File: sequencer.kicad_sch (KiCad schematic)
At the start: 68 parts, among them J1 AudioJack2, J2 AudioJack2_Switch, J3 AudioJack2, J4 Conn_ARM_JTAG_SWD_10, J5 Conn_01x06_Male, SW1 OS102011MS2QN1, SW10 OS102011MS2QN1, SW2 OS102011MS2QN1, SW3 OS102011MS2QN1, SW4 OS102011MS2QN1, SW5 OS102011MS2QN1, SW6 OS102011MS2QN1, SW7 OS102011MS2QN1, SW8 OS102011MS2QN1, U1 LM358, U2 74HC4051, U3 STM32F031K6Tx, U4 74HC14, U5 LM7805_TO220, U7 L78L33_SOT89, X1 ASV-8.000MHz

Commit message: Complete TODOs
- assign all footprints except pots
- hook up duty cycle pot
- add power switch
- switch to HCT inverters for logic level compatibility with 3.3V CMOS
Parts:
- removed J1, J3: AudioJack2, symbol Connector_Audio:AudioJack2
- removed J2: AudioJack2_Switch, symbol Connector_Audio:AudioJack2_Switch
- removed U5: LM7805_TO220, Package_TO_SOT_THT:TO-220-3_Vertical, symbol Regulator_Linear:LM7805_TO220
- added C27, C29, C31: 100n, Capacitor_SMD:C_0603_1608Metric, symbol Device:C
- added C28, C30: 330n, Capacitor_SMD:C_0805_2012Metric, symbol Device:C
- added J1, J2, J3: AudioJack2_SwitchT, Connector_Audio:Jack_3.5mm_QingPu_WQP-PJ398SM_Vertical_CircularHoles, symbol Connector_Audio:AudioJack2_SwitchT
- added J6: Conn_01x02_Male, Connector_Molex:Molex_SL_171971-0002_1x02_P2.54mm_Vertical, symbol Connector:Conn_01x02_Male
- added RV10: 10k, symbol Device:R_Potentiometer
- added SW10: SW_SPST, Button_Switch_THT_gkeeth:SW_Toggle_SPST_NKK_M2011xxx03, symbol Switch:SW_SPST
- added U5: L78L05_SOT89, Package_TO_SOT_SMD:SOT-89-3, symbol Regulator_Linear:L78L05_SOT89
- D9: footprint LED_SMD:LED_0603_1608Metric_Castellated -> LED_SMD:LED_0603_1608Metric
- J5: footprint (none) -> Connector_PinHeader_2.54mm:PinHeader_1x06_P2.54mm_Vertical
- U1: footprint (none) -> Package_SO:SOIC-8_3.9x4.9mm_P1.27mm
- U2: footprint (none) -> Package_SO:SOIC-16_3.9x9.9mm_P1.27mm
- U4: value 74HC14 -> 74HCT14; footprint (none) -> Package_SO:SOIC-14_3.9x8.7mm_P1.27mm
- renumbered C13 to C26, SW10 to SW9, U7 to U6
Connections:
- net clock_out_unbuffered is gone; now on net selected_clock_buffered: U4.5
- net +3.3V: now also U6.1 (OUT), C31.2, RV10.1
- net +5V: now also SW9.1 (A), C29.2, U5.1 (OUT)
- net +9V: now also U6.3 (IN), C28.1, C30.1, SW10.2 (B), U5.3 (IN)
- net GND: now also SW9.3 (C), U6.2 (GND), C27.1, C28.2, C29.1, C30.2, C31.1, J1.S, J2.S, J3.S, J6.2 (Pin_2), RV10.3, U5.2 (GND)
- net clock_out_buffered: now also J3.T
- net cv_out_buffered: now also J2.T
- net internal_clock: now also U3.21 (PA11), J1.TN; no longer U3.14 (PB0)
- net selected_clock_unbuffered: now also J1.T
- net skip_reset_switch: now reaches SW9.2 (B)
- net skip_reset_switch: now also U3.18 (PA8)
- new net: J6.1 (Pin_1), SW10.1 (A)
- new net duty_pot: C27.2, RV10.2, U3.14 (PB0)
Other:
- note added: "ADC_IN8"
- note added: "CV Output"
- note added: "Clock Input"
- note added: "Clock/Gate Output"
- note added: "Gate Duty Cycle Control"
- note added: "Power Switch"
- note added: "Skip/Reset Selector"
- note added: "TIM1_CH4"
- note added: "Tempo Control"
- note removed: "TIM3_CH3"
- moved on the sheet: C26, J4, R3, RV9, SW9, U4A, U4B, U4C, U4D, U6

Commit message: add footprints to pots
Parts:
- RV1, RV10, RV2, RV3, RV4, RV5, RV6, RV7, RV8, RV9: footprint (none) -> Potentiometer_THT:Potentiometer_Bourns_PTV09A-1_Single_Vertical; Distributor (none) -> Digikey; Distributor PN (none) -> PTV09A-4020F-B103-ND; Manufacturer (none) -> Bourns; Manufacturer PN (none) -> PTV09A-4020F-B103
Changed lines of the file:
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@@
       (effects (font (size 1.27 1.27)) (justify right))
     )
-    (property "Footprint" "" (at 93.98 26.67 0)
+    (property "Footprint" "Potentiometer_THT:Potentiometer_Bourns_PTV09A-1_Single_Vertical" (at 93.98 26.67 0)
       (effects (font (size 1.27 1.27)) hide)
     )
@@
       (effects (font (size 1.27 1.27)) hide)
     )
+    (property "Distributor" "Digikey" (at 93.98 26.67 0)
+      (effects (font (size 1.27 1.27)) hide)
+    )
+    (property "Distributor PN" "PTV09A-4020F-B103-ND" (at 93.98 26.67 0)
+      (effects (font (size 1.27 1.27)) hide)
+    )
+    (property "Manufacturer" "Bourns" (at 93.98 26.67 0)
+      (effects (font (size 1.27 1.27)) hide)
+    )
+    (property "Manufacturer PN" "PTV09A-4020F-B103" (at 93.98 26.67 0)
+      (effects (font (size 1.27 1.27)) hide)
+    )
     (pin "1")
     (pin "2")
@@
       (effects (font (size 1.27 1.27)) (justify right))
     )
-    (property "Footprint" "" (at 252.73 26.67 0)
+    (property "Footprint" "Potentiometer_THT:Potentiometer_Bourns_PTV09A-1_Single_Vertical" (at 252.73 26.67 0)
       (effects (font (size 1.27 1.27)) hide)
     )
@@
       (effects (font (size 1.27 1.27)) hide)
     )
+    (property "Distributor" "Digikey" (at 252.73 26.67 0)
+      (effects (font (size 1.27 1.27)) hide)
+    )
+    (property "Distributor PN" "PTV09A-4020F-B103-ND" (at 252.73 26.67 0)
+      (effects (font (size 1.27 1.27)) hide)
+    )
+    (property "Manufacturer" "Bourns" (at 252.73 26.67 0)
+      (effects (font (size 1.27 1.27)) hide)
+    )
+    (property "Manufacturer PN" "PTV09A-4020F-B103" (at 252.73 26.67 0)
+      (effects (font (size 1.27 1.27)) hide)
+    )
     (pin "1")
     (pin "2")
@@
       (effects (font (size 1.27 1.27)) (justify right))
     )
-    (property "Footprint" "" (at 62.23 26.67 0)
+    (property "Footprint" "Potentiometer_THT:Potentiometer_Bourns_PTV09A-1_Single_Vertical" (at 62.23 26.67 0)
       (effects (font (size 1.27 1.27)) hide)
     )
@@
       (effects (font (size 1.27 1.27)) hide)
     )
+    (property "Distributor" "Digikey" (at 62.23 26.67 0)
+      (effects (font (size 1.27 1.27)) hide)
+    )
+    (property "Distributor PN" "PTV09A-4020F-B103-ND" (at 62.23 26.67 0)
+      (effects (font (size 1.27 1.27)) hide)
+    )
+    (property "Manufacturer" "Bourns" (at 62.23 26.67 0)
+      (effects (font (size 1.27 1.27)) hide)
+    )
+    (property "Manufacturer PN" "PTV09A-4020F-B103" (at 62.23 26.67 0)
+      (effects (font (size 1.27 1.27)) hide)
+    )
     (pin "1")
     (pin "2")
@@
       (effects (font (size 1.27 1.27)) (justify right))
     )
-    (property "Footprint" "" (at 220.98 26.67 0)
+    (property "Footprint" "Potentiometer_THT:Potentiometer_Bourns_PTV09A-1_Single_Vertical" (at 220.98 26.67 0)
       (effects (font (size 1.27 1.27)) hide)
     )
@@
       (effects (font (size 1.27 1.27)) hide)
     )
+    (property "Distributor" "Digikey" (at 220.98 26.67 0)
+      (effects (font (size 1.27 1.27)) hide)
+    )
+    (property "Distributor PN" "PTV09A-4020F-B103-ND" (at 220.98 26.67 0)
+      (effects (font (size 1.27 1.27)) hide)
+    )
+    (property "Manufacturer" "Bourns" (at 220.98 26.67 0)
+      (effects (font (size 1.27 1.27)) hide)
+    )
+    (property "Manufacturer PN" "PTV09A-4020F-B103" (at 220.98 26.67 0)
+      (effects (font (size 1.27 1.27)) hide)
+    )
     (pin "1")
     (pin "2")
@@
       (effects (font (size 1.27 1.27)) (justify right))
     )
-    (property "Footprint" "" (at 125.73 26.67 0)
+    (property "Footprint" "Potentiometer_THT:Potentiometer_Bourns_PTV09A-1_Single_Vertical" (at 125.73 26.67 0)
       (effects (font (size 1.27 1.27)) hide)
     )
@@
       (effects (font (size 1.27 1.27)) hide)
     )
+    (property "Distributor" "Digikey" (at 125.73 26.67 0)
+      (effects (font (size 1.27 1.27)) hide)
+    )
+    (property "Distributor PN" "PTV09A-4020F-B103-ND" (at 125.73 26.67 0)
+      (effects (font (size 1.27 1.27)) hide)
+    )
+    (property "Manufacturer" "Bourns" (at 125.73 26.67 0)
+      (effects (font (size 1.27 1.27)) hide)
+    )
+    (property "Manufacturer PN" "PTV09A-4020F-B103" (at 125.73 26.67 0)
+      (effects (font (size 1.27 1.27)) hide)
+    )
     (pin "1")
     (pin "2")
@@
       (effects (font (size 1.27 1.27)) (justify right))
     )
-    (property "Footprint" "" (at 30.48 168.91 0)
+    (property "Footprint" "Potentiometer_THT:Potentiometer_Bourns_PTV09A-1_Single_Vertical" (at 30.48 168.91 0)
       (effects (font (size 1.27 1.27)) hide)
     )
@@
       (effects (font (size 1.27 1.27)) hide)
     )
+    (property "Distributor" "Digikey" (at 30.48 168.91 0)
+      (effects (font (size 1.27 1.27)) hide)
+    )
+    (property "Distributor PN" "PTV09A-4020F-B103-ND" (at 30.48 168.91 0)
+      (effects (font (size 1.27 1.27)) hide)
+    )
+    (property "Manufacturer" "Bourns" (at 30.48 168.91 0)
+      (effects (font (size 1.27 1.27)) hide)
+    )
+    (property "Manufacturer PN" "PTV09A-4020F-B103" (at 30.48 168.91 0)
+      (effects (font (size 1.27 1.27)) hide)
+    )
     (pin "1")
     (pin "2")
@@
       (effects (font (size 1.27 1.27)) (justify right))
     )
-    (property "Footprint" "" (at 30.48 26.67 0)
+    (property "Footprint" "Potentiometer_THT:Potentiometer_Bourns_PTV09A-1_Single_Vertical" (at 30.48 26.67 0)
       (effects (font (size 1.27 1.27)) hide)
     )
@@
       (effects (font (size 1.27 1.27)) hide)
     )
+    (property "Distributor" "Digikey" (at 30.48 26.67 0)
+      (effects (font (size 1.27 1.27)) hide)
+    )
+    (property "Distributor PN" "PTV09A-4020F-B103-ND" (at 30.48 26.67 0)
+      (effects (font (size 1.27 1.27)) hide)
+    )
+    (property "Manufacturer" "Bourns" (at 30.48 26.67 0)
+      (effects (font (size 1.27 1.27)) hide)
+    )
+    (property "Manufacturer PN" "PTV09A-4020F-B103" (at 30.48 26.67 0)
+      (effects (font (size 1.27 1.27)) hide)
+    )
     (pin "1")
     (pin "2")
@@
       (effects (font (size 1.27 1.27)) (justify right))
     )
-    (property "Footprint" "" (at 80.01 168.91 0)
+    (property "Footprint" "Potentiometer_THT:Potentiometer_Bourns_PTV09A-1_Single_Vertical" (at 80.01 168.91 0)
       (effects (font (size 1.27 1.27)) hide)
     )
@@
       (effects (font (size 1.27 1.27)) hide)
     )
+    (property "Distributor" "Digikey" (at 80.01 168.91 0)
+      (effects (font (size 1.27 1.27)) hide)
+    )
+    (property "Distributor PN" "PTV09A-4020F-B103-ND" (at 80.01 168.91 0)
+      (effects (font (size 1.27 1.27)) hide)
+    )
+    (property "Manufacturer" "Bourns" (at 80.01 168.91 0)
+      (effects (font (size 1.27 1.27)) hide)
+    )
+    (property "Manufacturer PN" "PTV09A-4020F-B103" (at 80.01 168.91 0)
+      (effects (font (size 1.27 1.27)) hide)
+    )
     (pin "1")
     (pin "2")
@@
       (effects (font (size 1.27 1.27)) (justify right))
     )
-    (property "Footprint" "" (at 189.23 26.67 0)
+    (property "Footprint" "Potentiometer_THT:Potentiometer_Bourns_PTV09A-1_Single_Vertical" (at 189.23 26.67 0)
       (effects (font (size 1.27 1.27)) hide)
     )
@@
       (effects (font (size 1.27 1.27)) hide)
     )
+    (property "Distributor" "Digikey" (at 189.23 26.67 0)
+      (effects (font (size 1.27 1.27)) hide)
+    )
+    (property "Distributor PN" "PTV09A-4020F-B103-ND" (at 189.23 26.67 0)
+      (effects (font (size 1.27 1.27)) hide)
+    )
+    (property "Manufacturer" "Bourns" (at 189.23 26.67 0)
+      (effects (font (size 1.27 1.27)) hide)
+    )
+    (property "Manufacturer PN" "PTV09A-4020F-B103" (at 189.23 26.67 0)
+      (effects (font (size 1.27 1.27)) hide)
+    )
     (pin "1")
     (pin "2")
@@
       (effects (font (size 1.27 1.27)) (justify right))
     )
-    (property "Footprint" "" (at 157.48 26.67 0)
+    (property "Footprint" "Potentiometer_THT:Potentiometer_Bourns_PTV09A-1_Single_Vertical" (at 157.48 26.67 0)
       (effects (font (size 1.27 1.27)) hide)
     )
@@
       (effects (font (size 1.27 1.27)) hide)
     )
+    (property "Distributor" "Digikey" (at 157.48 26.67 0)
+      (effects (font (size 1.27 1.27)) hide)
+    )
+    (property "Distributor PN" "PTV09A-4020F-B103-ND" (at 157.48 26.67 0)
+      (effects (font (size 1.27 1.27)) hide)
+    )
+    (property "Manufacturer" "Bourns" (at 157.48 26.67 0)
+      (effects (font (size 1.27 1.27)) hide)
+    )
+    (property "Manufacturer PN" "PTV09A-4020F-B103" (at 157.48 26.67 0)
+      (effects (font (size 1.27 1.27)) hide)
+    )

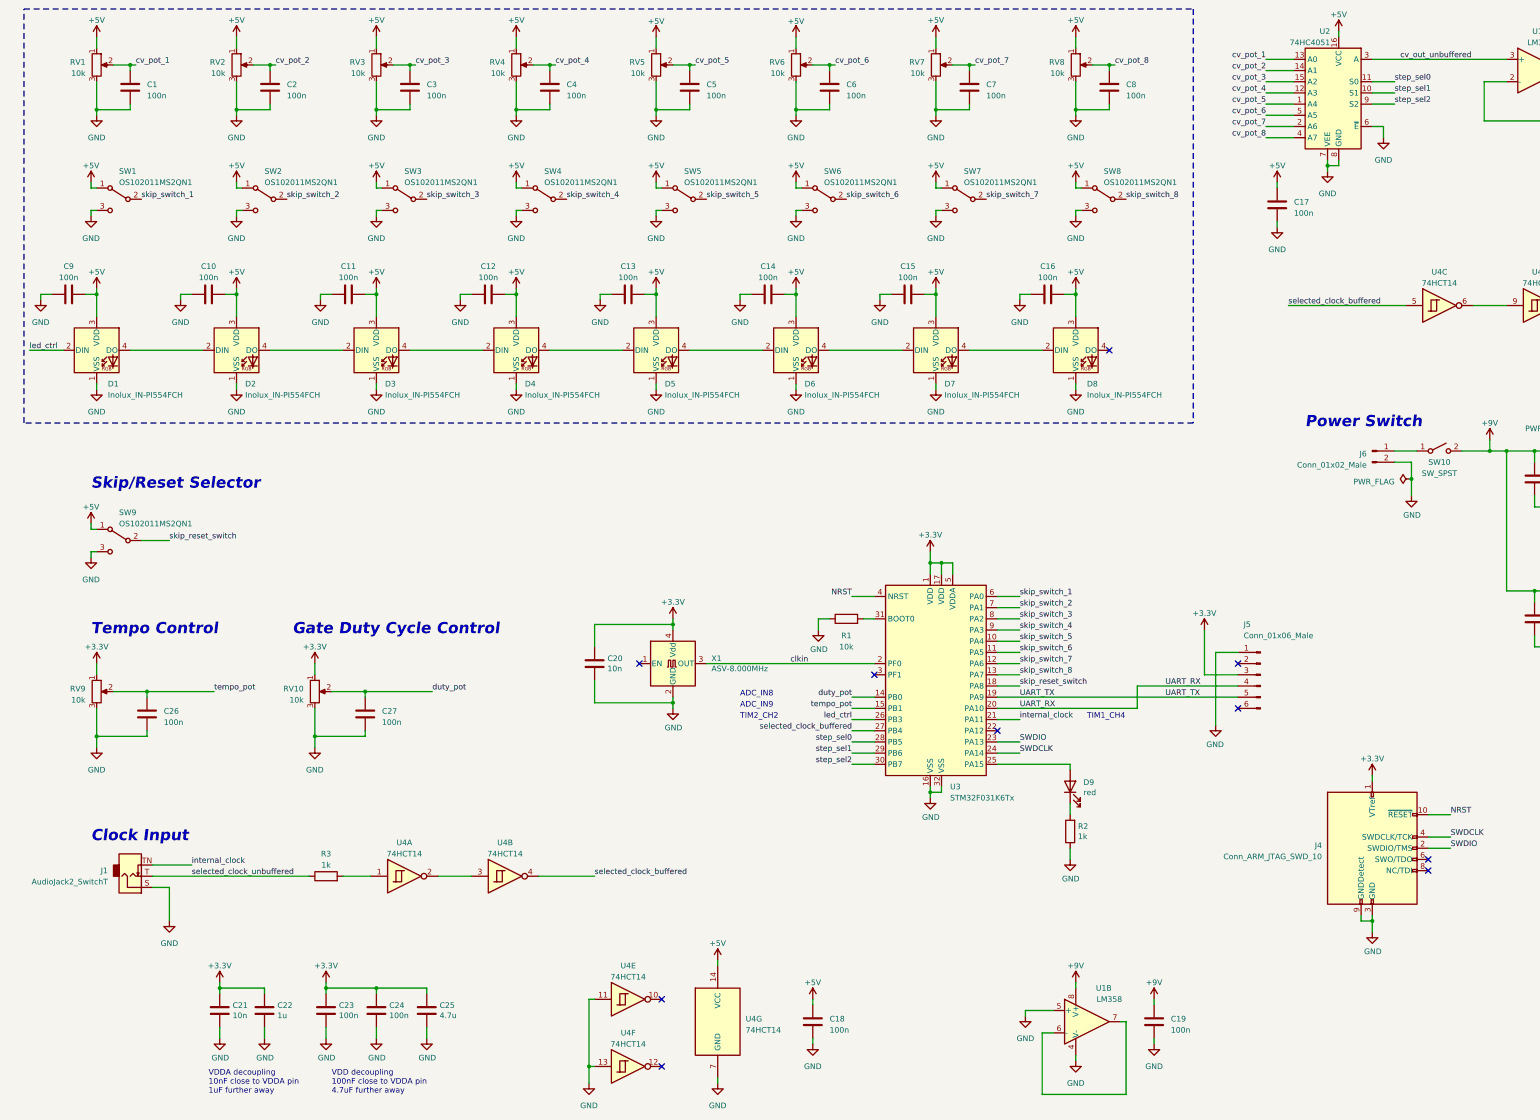
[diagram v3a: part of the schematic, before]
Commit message: initial routing complete, DRC errors clean
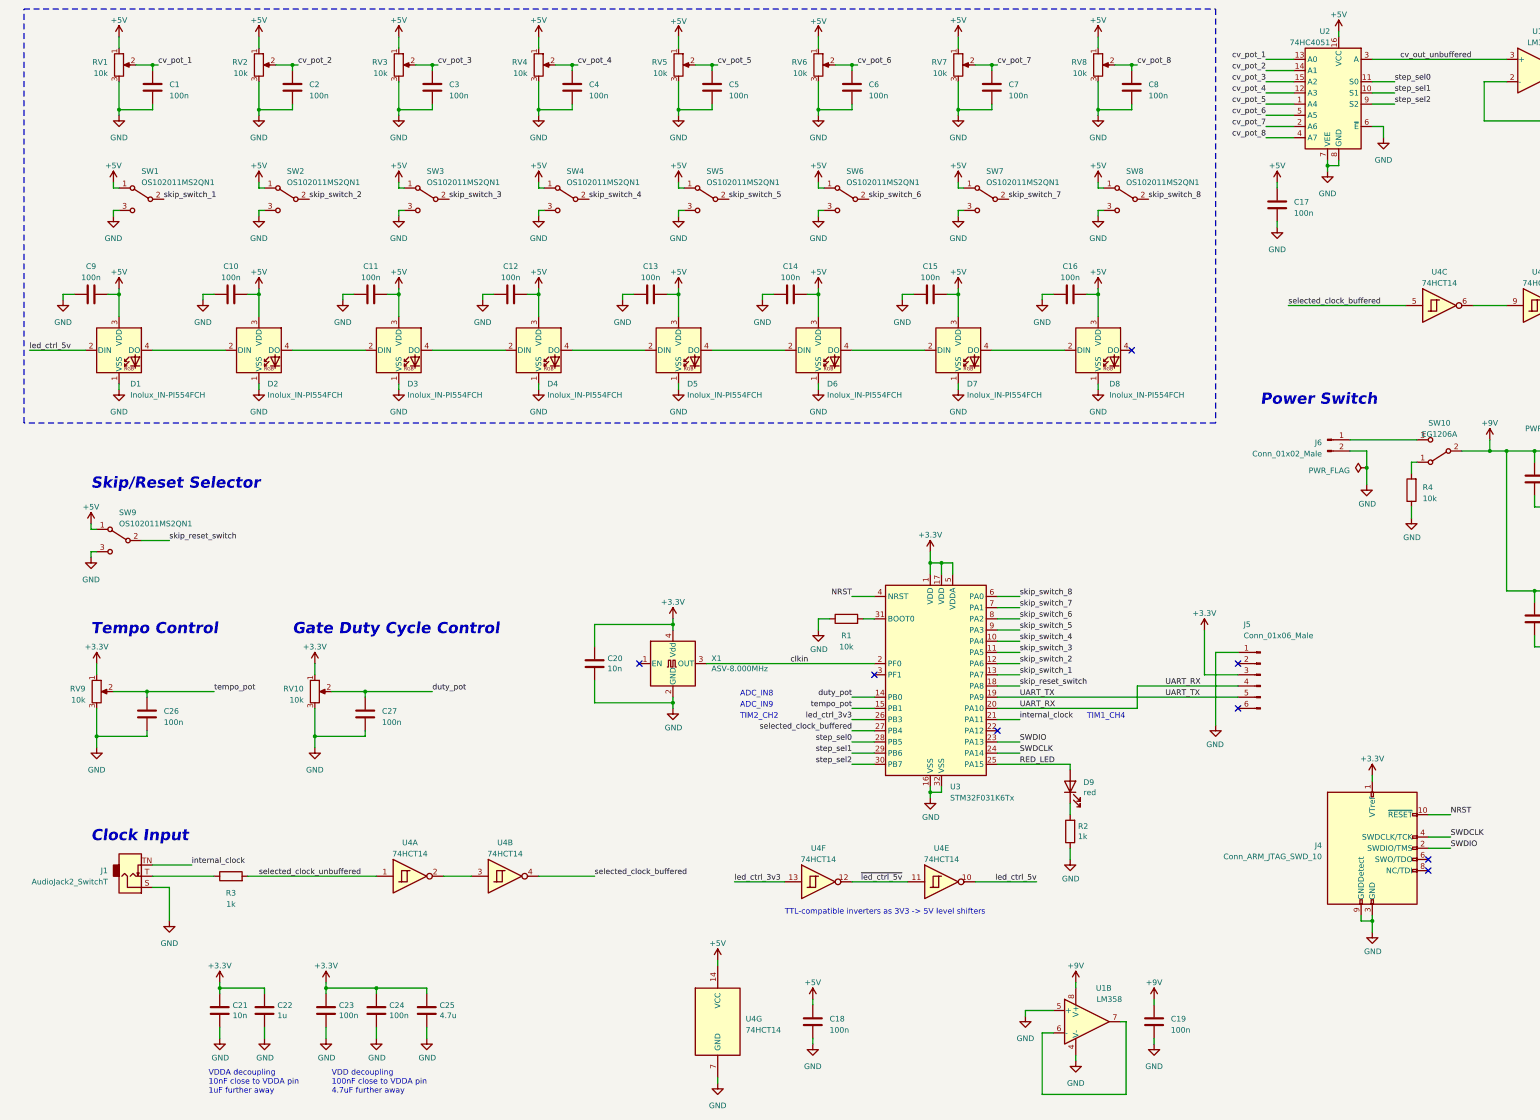
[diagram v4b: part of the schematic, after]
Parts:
- added R4: 10k, Resistor_SMD:R_0603_1608Metric, symbol Device:R
- J5: footprint Connector_PinHeader_2.54mm:PinHeader_1x06_P2.54mm_Vertical -> Connector_PinHeader_2.54mm:PinHeader_1x06_P2.54mm_Horizontal
- J6: footprint Connector_Molex:Molex_SL_171971-0002_1x02_P2.54mm_Vertical -> Connector_Molex_SL:Molex_SL_A-70553-0001_1x02_P2.54mm_Horizontal
- SW10: value SW_SPST -> EG1206A; footprint Button_Switch_THT_gkeeth:SW_Toggle_SPST_NKK_M2011xxx03 -> Button_Switch_THT_gkeeth:SW_Slide_SPDT_E-Switch_EG1206A; symbol Switch:SW_SPST -> Switch:SW_SPDT; Manufacturer (none) -> E-switch; Manufacturer PN (none) -> EG1206A
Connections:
- net GND: now also R4.1; no longer U4.11, U4.13
- net selected_clock_unbuffered: now also R3.2, U4.1; no longer J1.T, R3.1
- net skip_switch_1: now also U3.13 (PA7); no longer U3.6 (PA0)
- net skip_switch_2: now also U3.12 (PA6); no longer U3.7 (PA1)
- net skip_switch_3: now also U3.11 (PA5); no longer U3.8 (PA2)
- net skip_switch_4: now also U3.10 (PA4); no longer U3.9 (PA3)
- net skip_switch_5: now also U3.9 (PA3); no longer U3.10 (PA4)
- net skip_switch_6: now also U3.8 (PA2); no longer U3.11 (PA5)
- net skip_switch_7: now also U3.7 (PA1); no longer U3.12 (PA6)
- net skip_switch_8: now also U3.6 (PA0); no longer U3.13 (PA7)
- net RED_LED: now reaches D9.2 (A), U3.25 (PA15)
- net led_ctrl_5v: now reaches U4.10
- net led_ctrl_5v: now also D1.2 (DIN)
- net at J6.1 (Pin_1): now also SW10.3 (C); no longer SW10.1 (A)
- net ~{led_ctrl_5v}: now reaches U4.12
- net ~{led_ctrl_5v}: now also U4.11
- net led_ctrl renamed led_ctrl_3v3
- net led_ctrl_3v3: now also U4.13; no longer D1.2 (DIN)
- new net: R4.2, SW10.1 (A)
- new net: J1.T, R3.1
- no-connect marks 12 -> 10
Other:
- note added: "TTL-compatible inverters as 3V3 -> 5V level shifters"
- moved on the sheet: C1, C10, C11, C12, C13, C14, C15, C16, C2, C3, C4, C5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

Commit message: Circuit fixes and cleanup
- minor schematic rearranging
- checking I/O levels between MCU and 5V logic (still need to check
  switch selection bits)
- change switches to 3V3, re-route
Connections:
- net +3.3V: now also SW1.1 (A), SW2.1 (A), SW3.1 (A), SW4.1 (A), SW5.1 (A), SW6.1 (A), SW7.1 (A), SW8.1 (A), SW9.1 (A)
- net +5V: no longer SW1.1 (A), SW2.1 (A), SW3.1 (A), SW4.1 (A), SW5.1 (A), SW6.1 (A), SW7.1 (A), SW8.1 (A), SW9.1 (A)
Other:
- note added: "PB4 is 5V-tolerant"
- moved on the sheet: C18, C20, C21, C22, C23, C24, C25, J4, SW9, U1B, U4E, U4F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
